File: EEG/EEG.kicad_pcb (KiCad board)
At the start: 2 copper layers, 100 x 50 mm, 45 parts, among them J1 USB_B_Micro, J2 Conn_01x08_Female, J3 Conn_01x08_Female, Q1 SS8050, Q2 SS8050, SW1 SW_Push, SW2 SW_Push, U1 AMS1117-3.3, U2 FT231XS, U3 ESP32-PICO-D4, U4 MAX7219

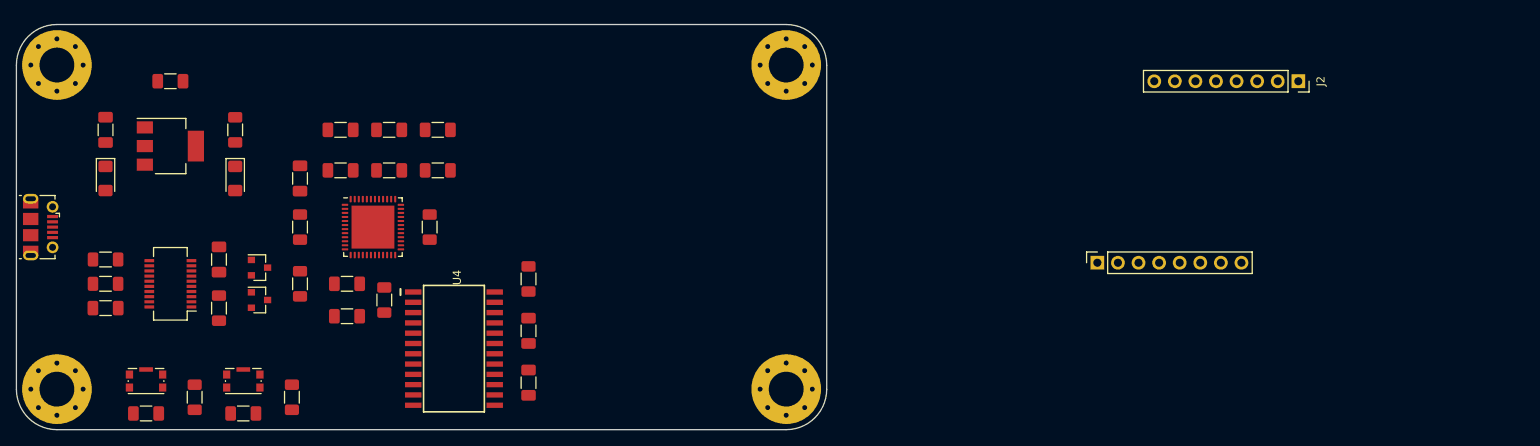
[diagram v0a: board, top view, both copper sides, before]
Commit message: updated sch for led conn
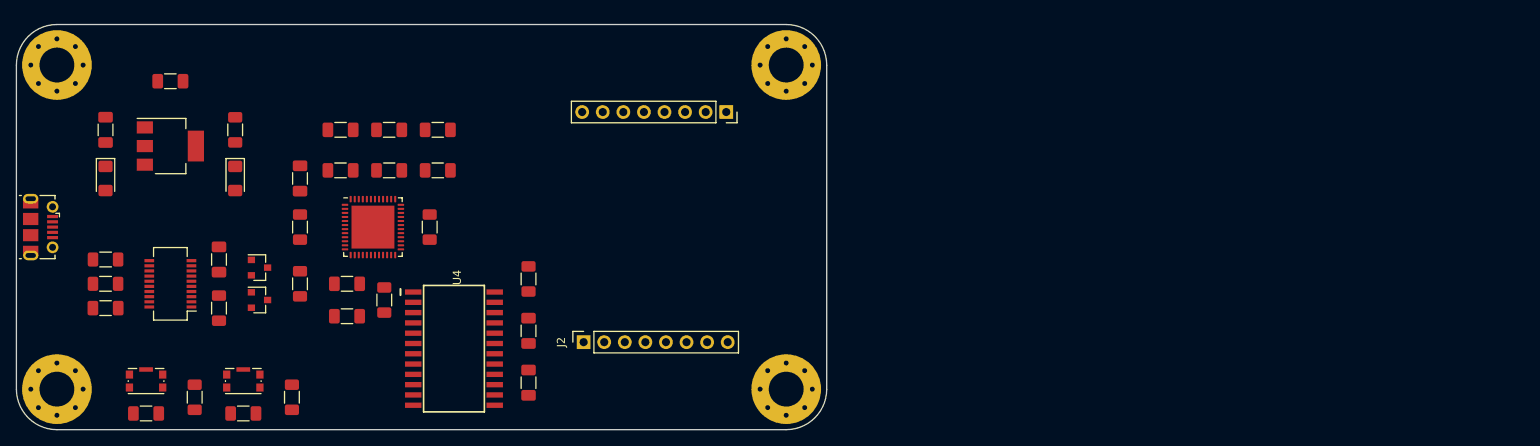
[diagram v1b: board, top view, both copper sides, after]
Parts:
- moved J2 93.9 mm to (87.0, 105.2), turned to 90 degrees
- moved J3 49.4 mm to (104.6, 76.8), turned to 270 degrees
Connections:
- J2 pad 1: SEGDP -> DIG4
- J2 pad 2: SEGA -> DIG6
- J2 pad 3: SEGB -> SEGA
- J2 pad 4: SEGC -> SEGB
- J2 pad 5: SEGD -> DIG7
- J2 pad 6: SEGE -> SEGD
- J2 pad 7: SEGF -> DIG5
- J2 pad 8: SEGG -> DIG2
- J3 pad 1: DIG7 -> DIG0
- J3 pad 2: DIG6 -> SEGC
- J3 pad 3: DIG5 -> SEGE
- J3 pad 4: DIG4 -> DIG3
- J3 pad 5: DIG3 -> SEGDP
- J3 pad 6: DIG2 -> DIG1
- J3 pad 7: DIG1 -> SEGF
- J3 pad 8: DIG0 -> SEGG
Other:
- copper layers 2 -> 4

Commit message: added some route
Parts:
- moved C11 86.0 mm to (143.8, 97.0)
- moved C17 86.0 mm to (143.8, 101.0)
- moved C1 86.0 mm to (114.0, 100.0)
- moved C10 86.0 mm to (143.0, 83.0)
- moved C12 86.0 mm to (155.0, 83.0)
- moved C13 86.0 mm to (149.0, 83.0)
- moved C14 86.0 mm to (155.0, 78.0)
- moved C15 86.0 mm to (149.0, 78.0)
- moved C16 86.0 mm to (143.0, 78.0)
- moved C2 86.0 mm to (114.0, 78.0)
- moved C3 86.0 mm to (122.0, 72.0)
- moved C4 86.0 mm to (119.0, 113.0)
- moved C5 86.0 mm to (131.0, 113.0)
- moved C6 86.0 mm to (128.0, 94.0)
- moved C7 86.0 mm to (138.0, 84.0)
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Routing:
- net GND: track 0.00 -> 79.0 mm, vias 0 -> 18
- net +3V3: track 0.00 -> 73.6 mm, vias 0 -> 7
- net EN: track 0.00 -> 48.7 mm, vias 0 -> 2
- net IO0: track 0.00 -> 35.6 mm, vias 0 -> 2
- net Net-(C6-Pad1): track 0.00 -> 16.0 mm, vias 0 -> 2
- net Net-(C5-Pad1): track 0.00 -> 13.4 mm
- net Net-(C4-Pad1): track 0.00 -> 13.1 mm
- net D-: track 0.00 -> 11.2 mm
- net Net-(Q1-Pad1): track 0.00 -> 10.0 mm
- net Net-(Q1-Pad2): track 0.00 -> 9.29 mm, vias 0 -> 1
- net Net-(Q2-Pad1): track 0.00 -> 8.42 mm
- net Net-(C2-Pad1): track 0.00 -> 7.89 mm
- net Net-(D1-Pad2): track 0.00 -> 7.87 mm
- net D+: track 0.00 -> 6.78 mm, vias 0 -> 1
- net Net-(Q2-Pad2): track 0.00 -> 5.04 mm
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- added copper zone on In1.Cu, net +3V3
- added copper zone on In2.Cu, net GND

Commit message: added more trace
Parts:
- moved C8 21.0 mm to (145.3, 110.7)
- turned U4 to 90 degrees
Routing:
- net SEGC: track 0.00 -> 79.2 mm, vias 0 -> 2
- net SEGE: track 0.00 -> 51.9 mm, vias 0 -> 2
- net SEGDP: track 0.00 -> 50.4 mm, vias 0 -> 1
- net SEGF: track 0.00 -> 49.3 mm, vias 0 -> 1
- net RXD: track 1.87 -> 42.7 mm, vias 1 -> 2
- net DIG3: track 0.00 -> 38.3 mm, vias 0 -> 1
- net SEGG: track 0.00 -> 38.2 mm, vias 0 -> 1
- net +3V3: track 73.6 -> 108.4 mm, vias 7 -> 16
- net Data: track 0.00 -> 34.8 mm, vias 0 -> 2
- net TXD: track 0.00 -> 32.7 mm, vias 0 -> 2
- net DIG1: track 0.00 -> 30.8 mm, vias 0 -> 1
- net GND: track 79.0 -> 107.9 mm, vias 18 -> 28
- net Sclk: track 0.00 -> 14.0 mm, vias 0 -> 2
- net Net-(J1-Pad6): track 0.00 -> 12.4 mm
- net CS: track 0.00 -> 5.40 mm
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
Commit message: Finished routing
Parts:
- added R12: 2K, Resistor_SMD:R_1206_3216Metric_Pad1.30x1.75mm_HandSolder, F.Cu at (118.2, 87.6)
- added Test: LED, LED_SMD:LED_1206_3216Metric_Pad1.42x1.75mm_HandSolder, F.Cu at (121.5, 87.6)
- moved R10 27.7 mm to (140.2, 106.0)
- moved C9 19.6 mm to (148.3, 110.7)
- moved Power 0.51 mm to (130.1, 83.5)
- renumbered D2 to Power
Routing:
- net SEGB: track 0.00 -> 50.7 mm, vias 0 -> 2
- net DIG0: track 0.00 -> 48.0 mm, vias 0 -> 1
- net SEGA: track 0.00 -> 39.3 mm
- net SEGD: track 0.00 -> 39.2 mm
- net DIG2: track 0.00 -> 31.7 mm, vias 0 -> 1
- net Net-(Q2-Pad1): track 8.42 -> 39.3 mm, vias 0 -> 2
- net DIG5: track 0.00 -> 29.8 mm
- net GND: track 107.9 -> 137.3 mm, vias 28 -> 40
- net Net-(D3-Pad2): track 0.00 -> 28.2 mm, vias 0 -> 2
- net DIG7: track 0.00 -> 25.7 mm, vias 0 -> 2
- net +3V3: track 108.4 -> 126.2 mm, vias 16 -> 19
- net DIG6: track 0.00 -> 14.6 mm
- net Net-(R10-Pad1): track 0.00 -> 13.2 mm
- net DIG4: track 0.00 -> 13.1 mm, vias 0 -> 1
- net CS: track 5.40 -> 16.7 mm
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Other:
- board text added: "EEG"
- board text added: "Mohit Patel, Adam Schuhcknecht, Evan Fadanalli"
